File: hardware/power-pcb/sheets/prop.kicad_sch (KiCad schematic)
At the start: 10 parts, among them J6 Molex_MicroFit-3.0_4x1, U5 BTT_TMC5160T_Pro

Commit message: Added power pcb sch + design
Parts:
- removed C13: 10u, Capacitor_THT:CP_Radial_D5.0mm_P2.50mm, symbol Device:C_Small
- removed R18: 10k, Resistor_SMD:R_0805_2012Metric_Pad1.20x1.40mm_HandSolder, symbol Device:R
- C5: renamed from C18; value 470u_LowZ -> 330u_LowZ; footprint Capacitor_THT:CP_Radial_D8.0mm_P3.50mm -> Capacitor_THT:CP_Radial_D10.0mm_P5.00mm; MPN EEUFR1C182L -> EEUFR1V331U
- renumbered C12 to C6, C14 to C7, J6 to J9, R15 to R13, R16 to R14, R17 to R15, U5 to U4
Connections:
- net MA: now reaches U4.11 (A2)
- net MA: now also J9.4 (Pin_4); no longer J9.1 (Pin_1)
- net MB: now reaches J9.2 (Pin_2), U4.12 (A1)
- net MC: now reaches U4.13 (B2)
- net MC: now also J9.1 (Pin_1); no longer J9.3 (Pin_3)
- net MD: now reaches U4.14 (B1)
- net MD: now also J9.3 (Pin_3); no longer J9.4 (Pin_4)
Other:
- moved on the sheet: J9

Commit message: Post DRM adjustements and BOM referencing
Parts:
- C6, C7: MPN (none) -> CL21B104KBCNNND; Manufacturer (none) -> Samsung
- J9: MPN (none) -> 43045-0425; Manufacturer (none) -> Molex
- R13, R14, R15: MPN (none) -> CRCW080510K0FKEA; Manufacturer (none) -> Vishay
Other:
- title: Propulsion motor trigger -> Propulsion motor
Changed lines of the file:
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@@
 	(paper "A5")
 	(title_block
-		(title "Propulsion motor trigger")
-		(date "2025-12-30")
-		(rev "1")
+		(title "Propulsion motor")
+		(date "2026-03-04")
+		(rev "1.1")
 		(company "Game Team SLSC")
 	)
@@
 			)
 		)
+		(property "MPN" "CRCW080510K0FKEA"
+			(at 50.8 69.85 0)
+			(effects
+				(font
+					(size 1.27 1.27)
+				)
+				(hide yes)
+			)
+		)
+		(property "Manufacturer" "Vishay"
+			(at 50.8 69.85 0)
+			(effects
+				(font
+					(size 1.27 1.27)
+				)
+				(hide yes)
+			)
+		)
 		(pin "1"
 		)
@@
 			)
 		)
+		(property "MPN" "CRCW080510K0FKEA"
+			(at 52.07 81.28 0)
+			(effects
+				(font
+					(size 1.27 1.27)
+				)
+				(hide yes)
+			)
+		)
+		(property "Manufacturer" "Vishay"
+			(at 52.07 81.28 0)
+			(effects
+				(font
+					(size 1.27 1.27)
+				)
+				(hide yes)
+			)
+		)
 		(pin "1"
 		)
@@
 			)
 		)
+		(property "MPN" "CL21B104KBCNNND"
+			(at 55.88 46.99 0)
+			(effects
+				(font
+					(size 1.27 1.27)
+				)
+				(hide yes)
+			)
+		)
+		(property "Manufacturer" "Samsung"
+			(at 55.88 46.99 0)
+			(effects
+				(font
+					(size 1.27 1.27)
+				)
+				(hide yes)
+			)
+		)
 		(pin "1"
 		)
@@
 			)
 		)
+		(property "MPN" "CL21B104KBCNNND"
+			(at 50.8 54.61 0)
+			(effects
+				(font
+					(size 1.27 1.27)
+				)
+				(hide yes)
+			)
+		)
+		(property "Manufacturer" "Samsung"
+			(at 50.8 54.61 0)
+			(effects
+				(font
+					(size 1.27 1.27)
+				)
+				(hide yes)
+			)
+		)
 		(pin "1"
 		)
@@
 			)
 		)
+		(property "MPN" "43045-0425"
+			(at 119.38 68.58 0)
+			(effects
+				(font
+					(size 1.27 1.27)
+				)
+				(hide yes)
+			)
+		)
+		(property "Manufacturer" "Molex"
+			(at 119.38 68.58 0)
+			(effects
+				(font
+					(size 1.27 1.27)
+				)
+				(hide yes)
+			)
+		)
 		(pin "2"
 		)
@@
 			(at 49.53 91.44 0)
 			(effects
+				(font
+					(size 1.27 1.27)
+				)
+				(hide yes)
+			)
+		)
+		(property "MPN" "CRCW080510K0FKEA"
+			(at 49.53 91.44 0)
+			(effects
+				(font
+					(size 1.27 1.27)
+				)
+				(hide yes)
+			)
+		)
+		(property "Manufacturer" "Vishay"
+			(at 49.53 91.44 0)
+			(effects

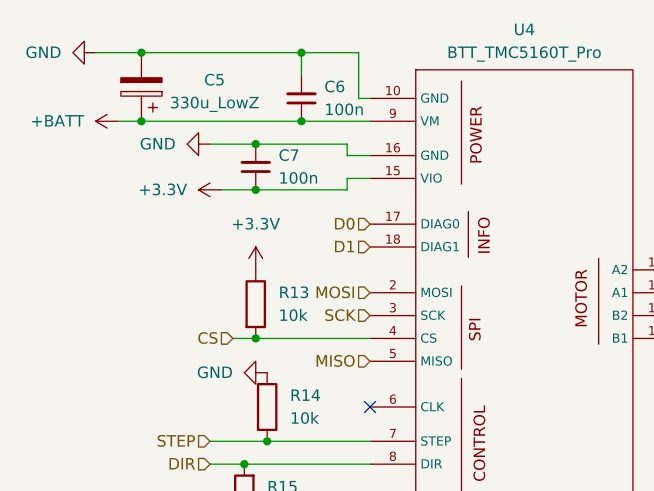
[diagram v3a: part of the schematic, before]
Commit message: Adapt Power PCB to logic requirements
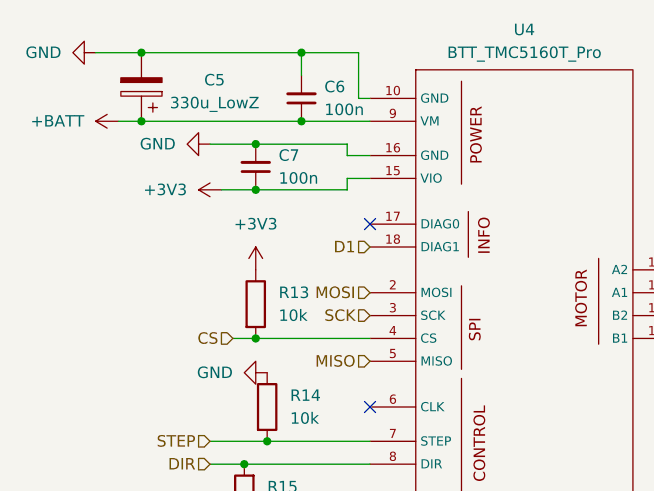
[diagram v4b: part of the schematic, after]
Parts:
- J9: footprint Project:Molex_Micro-Fit_3.0_43045-0412_2x02_P3.00mm_Vertical -> Project:J_Wurth_WR-MPC3_66200421122
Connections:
- net +3.3V renamed +3V3
- net D0: no longer names the net of U4.17 (DIAG0)
- no-connect marks 1 -> 2
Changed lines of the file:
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@@
 		(at 63.5 81.28)
+	)
+	(no_connect
+		(at 63.5 60.96)
 	)
 	(wire
@@
 		(shape input)
 		(at 60.96 92.71 180)
-		(effects
-			(font
-				(size 1.27 1.27)
-			)
-			(justify right)
-		)
-	)
-	(hierarchical_label "D0"
-		(shape input)
-		(at 63.5 60.96 180)
 		(effects
 			(font
@@
 	)
 	(symbol
-		(lib_id "power:+3.3V")
-		(at 46.99 57.15 90)
-		(unit 1)
-		(exclude_from_sim no)
-		(in_bom yes)
-		(on_board yes)
-		(dnp no)
-		(fields_autoplaced yes)
-		(property "Reference" "#PWR028"
-			(at 50.8 57.15 0)
-			(effects
-				(font
-					(size 1.27 1.27)
-				)
-				(hide yes)
-			)
-		)
-		(property "Value" "+3.3V"
-			(at 43.18 57.1499 90)
-			(effects
-				(font
-					(size 1.27 1.27)
-				)
-				(justify left)
-			)
-		)
-		(property "Footprint" ""
-			(at 46.99 57.15 0)
-			(effects
-				(font
-					(size 1.27 1.27)
-				)
-				(hide yes)
-			)
-		)
-		(property "Datasheet" ""
-			(at 46.99 57.15 0)
-			(effects
-				(font
-					(size 1.27 1.27)
-				)
-				(hide yes)
-			)
-		)
-		(property "Description" "Power symbol creates a global label with name \"+3.3V\""
-			(at 46.99 57.15 0)
-			(effects
-				(font
-					(size 1.27 1.27)
-				)
-				(hide yes)
-			)
-		)
-		(pin "1"
-		)
-		(instances
-			(project "eurobot-2026-robot-pcb"
-				(path "/52aa7d2f-6f25-4758-95ea-c8ad4c86433a/4e90b18c-b0f7-4f5c-916c-5e629142b1e8"
-					(reference "#PWR036")
-					(unit 1)
-				)
-				(path "/52aa7d2f-6f25-4758-95ea-c8ad4c86433a/becefb4a-e573-4ea9-a889-4d87c3f6029b"
-					(reference "#PWR044")
-					(unit 1)
-				)
-				(path "/52aa7d2f-6f25-4758-95ea-c8ad4c86433a/cb976dcc-9293-45e0-8c37-9341a8a408bc"
-					(reference "#PWR028")
-					(unit 1)
-				)
-				(path "/52aa7d2f-6f25-4758-95ea-c8ad4c86433a/ed4fc265-0747-46c1-ba83-bb82a792f24d"
-					(reference "#PWR052")
-					(unit 1)
-				)
-			)
-			(project "eurobot-2026-robot-pcb"
-				(path "/b7a41ac4-1d1a-4287-8cea-fdfe5ab5ee00/1a8703d8-5ba0-4c53-bb87-3353758fd726/2d3eda0e-5f7a-4d55-b4aa-645fd47dc899"
-					(reference "#PWR037")
-					(unit 1)
-				)
-				(path "/b7a41ac4-1d1a-4287-8cea-fdfe5ab5ee00/1a8703d8-5ba0-4c53-bb87-3353758fd726/643017f0-f26b-4b5a-a33b-fc1a99ef8d08"
-					(reference "#PWR0137")
-					(unit 1)
-				)
-				(path "/b7a41ac4-1d1a-4287-8cea-fdfe5ab5ee00/1a8703d8-5ba0-4c53-bb87-3353758fd726/683f7048-02be-4a56-bf88-b0b07ec401aa"
-					(reference "#PWR0153")
-					(unit 1)
-				)
-				(path "/b7a41ac4-1d1a-4287-8cea-fdfe5ab5ee00/1a8703d8-5ba0-4c53-bb87-3353758fd726/7031de1d-e161-4af6-b221-f84d5c8a02bd"
-					(reference "#PWR0145")
-					(unit 1)
-				)
-			)
-		)
-	)
-	(symbol
 		(lib_id "Device:R")
 		(at 50.8 69.85 0)
@@
 				(path "/b7a41ac4-1d1a-4287-8cea-fdfe5ab5ee00/1a8703d8-5ba0-4c53-bb87-3353758fd726/7031de1d-e161-4af6-b221-f84d5c8a02bd"
 					(reference "R51")
+					(unit 1)
+				)
+			)
+		)
+	)
+	(symbol
+		(lib_id "power:+3V3")
+		(at 46.99 57.15 90)
+		(unit 1)
+		(exclude_from_sim no)
+		(in_bom yes)
+		(on_board yes)
+		(dnp no)
+		(fields_autoplaced yes)
+		(property "Reference" "#PWR028"
+			(at 50.8 57.15 0)
+			(effects
+				(font
+					(size 1.27 1.27)
+				)
+				(hide yes)
+			)
+		)
+		(property "Value" "+3V3"
+			(at 43.18 57.1499 90)
+			(effects
+				(font
+					(size 1.27 1.27)
+				)
+				(justify left)
+			)
+		)
+		(property "Footprint" ""
+			(at 46.99 57.15 0)
+			(effects
+				(font
+					(size 1.27 1.27)
+				)
+				(hide yes)
+			)
+		)
+		(property "Datasheet" ""
+			(at 46.99 57.15 0)
+			(effects
+				(font
+					(size 1.27 1.27)
+				)
+				(hide yes)
+			)
+		)
+		(property "Description" "Power symbol creates a global label with name \"+3V3\""
+			(at 46.99 57.15 0)
+			(effects
+				(font
+					(size 1.27 1.27)
+				)
+				(hide yes)
+			)
+		)
+		(pin "1"
+		)
+		(instances
+			(project "power-pcb"
+				(path "/52aa7d2f-6f25-4758-95ea-c8ad4c86433a/4e90b18c-b0f7-4f5c-916c-5e629142b1e8"
+					(reference "#PWR036")
+					(unit 1)
+				)
+				(path "/52aa7d2f-6f25-4758-95ea-c8ad4c86433a/becefb4a-e573-4ea9-a889-4d87c3f6029b"
+					(reference "#PWR044")
+					(unit 1)
+				)
+				(path "/52aa7d2f-6f25-4758-95ea-c8ad4c86433a/cb976dcc-9293-45e0-8c37-9341a8a408bc"
+					(reference "#PWR028")
+					(unit 1)
+				)
+				(path "/52aa7d2f-6f25-4758-95ea-c8ad4c86433a/ed4fc265-0747-46c1-ba83-bb82a792f24d"
+					(reference "#PWR052")
+					(unit 1)
+				)
+			)
+		)
+	)
+	(symbol
+		(lib_id "power:+3V3")
+		(at 50.8 66.04 0)
+		(unit 1)
+		(exclude_from_sim no)
+		(in_bom yes)
+		(on_board yes)
+		(dnp no)
+		(fields_autoplaced yes)
+		(property "Reference" "#PWR029"
+			(at 50.8 69.85 0)
+			(effects
+				(font
+					(size 1.27 1.27)
+				)
+				(hide yes)
+			)
+		)
+		(property "Value" "+3V3"
+			(at 50.8 60.96 0)
+			(effects
+				(font
+					(size 1.27 1.27)
+				)
+			)
+		)
+		(property "Footprint" ""
+			(at 50.8 66.04 0)
+			(effects
+				(font
+					(size 1.27 1.27)
+				)
+				(hide yes)
+			)
+		)
+		(property "Datasheet" ""
+			(at 50.8 66.04 0)
+			(effects
+				(font
+					(size 1.27 1.27)
+				)
+				(hide yes)
+			)
+		)
+		(property "Description" "Power symbol creates a global label with name \"+3V3\""
+			(at 50.8 66.04 0)
+			(effects
+				(font
+					(size 1.27 1.27)
+				)
+				(hide yes)
+			)
+		)
+		(pin "1"
+		)
+		(instances
+			(project ""
+				(path "/52aa7d2f-6f25-4758-95ea-c8ad4c86433a/4e90b18c-b0f7-4f5c-916c-5e629142b1e8"
+					(reference "#PWR037")
+					(unit 1)
+				)
+				(path "/52aa7d2f-6f25-4758-95ea-c8ad4c86433a/becefb4a-e573-4ea9-a889-4d87c3f6029b"
+					(reference "#PWR045")
+					(unit 1)
+				)
+				(path "/52aa7d2f-6f25-4758-95ea-c8ad4c86433a/cb976dcc-9293-45e0-8c37-9341a8a408bc"
+					(reference "#PWR029")
+					(unit 1)
+				)
+				(path "/52aa7d2f-6f25-4758-95ea-c8ad4c86433a/ed4fc265-0747-46c1-ba83-bb82a792f24d"
+					(reference "#PWR053")
 					(unit 1)
 				)
@@
 			)
 		)
-		(property "Footprint" "Project:Molex_Micro-Fit_3.0_43045-0412_2x02_P3.00mm_Vertical"
+		(property "Footprint" "Project:J_Wurth_WR-MPC3_66200421122"
 			(at 119.38 68.58 0)
 			(effects
@@
 					(unit 1)
 				)
-			)
-		)
-	)
-	(symbol
-		(lib_id "power:+3.3V")
-		(at 50.8 66.04 0)
-		(unit 1)
-		(exclude_from_sim no)
-		(in_bom yes)
-		(on_board yes)
-		(dnp no)
-		(fields_autoplaced yes)
-		(property "Reference" "#PWR029"
-			(at 50.8 69.85 0)
-			(effects
-				(font
-					(size 1.27 1.27)
-				)
-				(hide yes)
-			)
-		)
-		(property "Value" "+3.3V"
-			(at 50.8 60.96 0)
-			(effects
-				(font
-					(size 1.27 1.27)
-				)
-			)
-		)
-		(property "Footprint" ""
-			(at 50.8 66.04 0)
-			(effects
-				(font
-					(size 1.27 1.27)
-				)
-				(hide yes)
-			)
-		)
-		(property "Datasheet" ""
-			(at 50.8 66.04 0)
-			(effects
-				(font
-					(size 1.27 1.27)
-				)
-				(hide yes)
-			)
-		)
-		(property "Description" "Power symbol creates a global label with name \"+3.3V\""
-			(at 50.8 66.04 0)
-			(effects
-				(font
-					(size 1.27 1.27)
-				)
-				(hide yes)
-			)
-		)
-		(pin "1"
-		)
-		(instances
-			(project "eurobot-2026-robot-pcb"
-				(path "/52aa7d2f-6f25-4758-95ea-c8ad4c86433a/4e90b18c-b0f7-4f5c-916c-5e629142b1e8"
-					(reference "#PWR037")
-					(unit 1)
-				)
-				(path "/52aa7d2f-6f25-4758-95ea-c8ad4c86433a/becefb4a-e573-4ea9-a889-4d87c3f6029b"
-					(reference "#PWR045")
-					(unit 1)
-				)
-				(path "/52aa7d2f-6f25-4758-95ea-c8ad4c86433a/cb976dcc-9293-45e0-8c37-9341a8a408bc"
-					(reference "#PWR029")
-					(unit 1)
-				)
-				(path "/52aa7d2f-6f25-4758-95ea-c8ad4c86433a/ed4fc265-0747-46c1-ba83-bb82a792f24d"
-					(reference "#PWR053")
-					(unit 1)
-				)
-			)
-			(project "eurobot-2026-robot-pcb"
-				(path "/b7a41ac4-1d1a-4287-8cea-fdfe5ab5ee00/1a8703d8-5ba0-4c53-bb87-3353758fd726/2d3eda0e-5f7a-4d55-b4aa-645fd47dc899"
-					(reference "#PWR040")
-					(unit 1)
-				)
-				(path "/b7a41ac4-1d1a-4287-8cea-fdfe5ab5ee00/1a8703d8-5ba0-4c53-bb87-3353758fd726/643017f0-f26b-4b5a-a33b-fc1a99ef8d08"
-					(reference "#PWR0140")
-					(unit 1)
-				)
-				(path "/b7a41ac4-1d1a-4287-8cea-fdfe5ab5ee00/1a8703d8-5ba0-4c53-bb87-3353758fd726/683f7048-02be-4a56-bf88-b0b07ec401aa"
-					(reference "#PWR0156")
-					(unit 1)
-				)
-				(path "/b7a41ac4-1d1a-4287-8cea-fdfe5ab5ee00/1a8703d8-5ba0-4c53-bb87-3353758fd726/7031de1d-e161-4af6-b221-f84d5c8a02bd"
-					(reference "#PWR0148")
-					(unit 1)
-				)

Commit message: fixes pre-prod
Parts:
- J9: MPN 43045-0425 -> 66200421122; Manufacturer Molex -> Wurth
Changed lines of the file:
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@@
 			)
 		)
-		(property "MPN" "43045-0425"
+		(property "MPN" "66200421122"
 			(at 119.38 68.58 0)
 			(effects
@@
 			)
 		)
-		(property "Manufacturer" "Molex"
+		(property "Manufacturer" "Wurth"
 			(at 119.38 68.58 0)
 			(effects
